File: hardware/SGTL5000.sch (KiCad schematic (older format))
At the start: 19 parts, among them J2 AudioJack3_Ground, U6 AP7313-1.8V, U7 SGTL5000

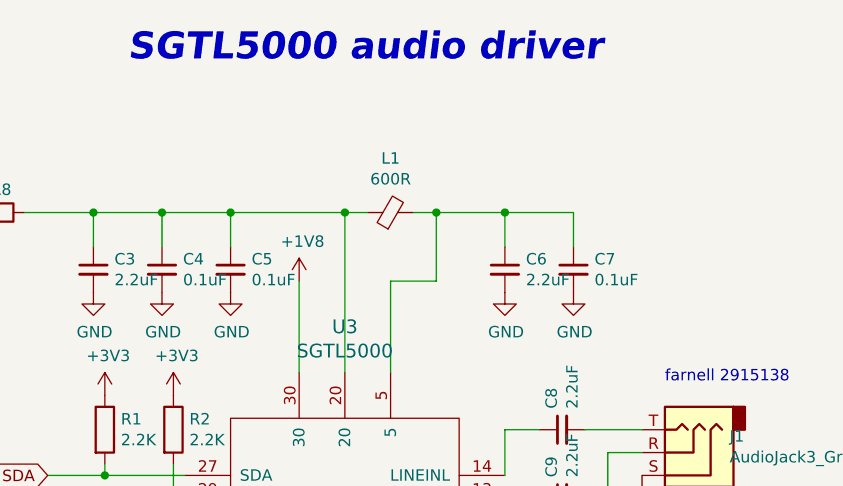
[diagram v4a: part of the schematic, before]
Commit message: new layout following feedback from pjrc forum
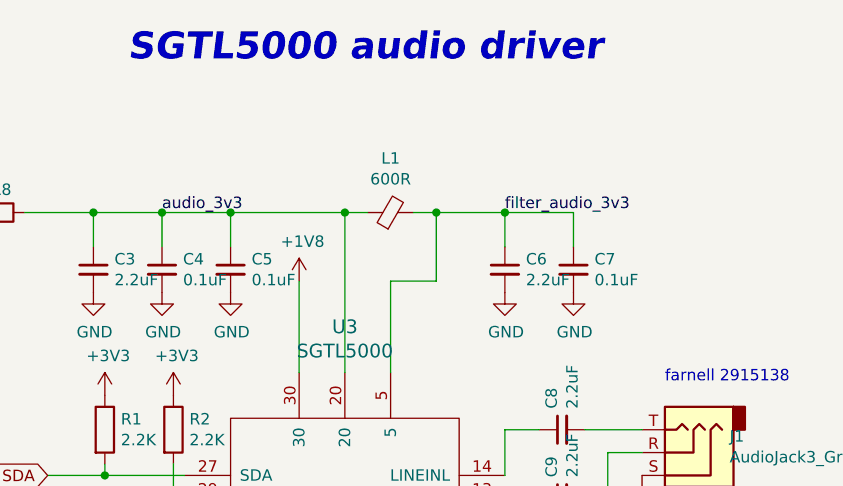
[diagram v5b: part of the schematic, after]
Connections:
- net audio_3v3: now reaches C26.1, C27.1, C28.1, L2.1, R8.1, U7.20
- net filter_audio_3v3: now reaches C29.1, C30.1, L2.2, U7.5
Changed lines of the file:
@@
-	1    0    0    -1
-$EndComp
-$Comp
-L power:GND #PWR?
-U 1 1 5BAC3E75
-P 4550 2350
-AR Path="/5BAC3E75" Ref="#PWR?"  Part="1"
-AR Path="/5BAC34FB/5BAC3E75" Ref="#PWR0128"  Part="1"
-AR Path="/5E0E3867/5BAC3E75" Ref="#PWR0108"  Part="1"
-F 0 "#PWR0108" H 4550 2100 50  0001 C CNN
-F 1 "GND" H 4555 2177 50  0000 C CNN
-F 2 "" H 4550 2350 50  0001 C CNN
-F 3 "" H 4550 2350 50  0001 C CNN
-	1    4550 2350
 	1    0    0    -1
 $EndComp
@@
 	1    0    0    -1
 $EndComp
-$Comp
-L power:GND #PWR?
-U 1 1 5BAC3E83
-P 4850 2350
-AR Path="/5BAC3E83" Ref="#PWR?"  Part="1"
-AR Path="/5BAC34FB/5BAC3E83" Ref="#PWR0129"  Part="1"
-AR Path="/5E0E3867/5BAC3E83" Ref="#PWR0109"  Part="1"
-F 0 "#PWR0109" H 4850 2100 50  0001 C CNN
-F 1 "GND" H 4855 2177 50  0000 C CNN
-F 2 "" H 4850 2350 50  0001 C CNN
-F 3 "" H 4850 2350 50  0001 C CNN
-	1    4850 2350
-	1    0    0    -1
-$EndComp
 Wire Wire Line
 	4850 2000 4850 2150
@@
 	1    0    0    -1
 $EndComp
-$Comp
-L power:GND #PWR?
-U 1 1 5BAC3E91
-P 5150 2350
-AR Path="/5BAC3E91" Ref="#PWR?"  Part="1"
-AR Path="/5BAC34FB/5BAC3E91" Ref="#PWR0130"  Part="1"
-AR Path="/5E0E3867/5BAC3E91" Ref="#PWR0110"  Part="1"
-F 0 "#PWR0110" H 5150 2100 50  0001 C CNN
-F 1 "GND" H 5155 2177 50  0000 C CNN
-F 2 "" H 5150 2350 50  0001 C CNN
-F 3 "" H 5150 2350 50  0001 C CNN
-	1    5150 2350
-	1    0    0    -1
-$EndComp
 Wire Wire Line
 	5150 2000 5150 2150
@@
 	1    0    0    -1
 $EndComp
-$Comp
-L power:GND #PWR?
-U 1 1 5BAC3E9F
-P 6350 2350
-AR Path="/5BAC3E9F" Ref="#PWR?"  Part="1"
-AR Path="/5BAC34FB/5BAC3E9F" Ref="#PWR0131"  Part="1"
-AR Path="/5E0E3867/5BAC3E9F" Ref="#PWR0111"  Part="1"
-F 0 "#PWR0111" H 6350 2100 50  0001 C CNN
-F 1 "GND" H 6355 2177 50  0000 C CNN
-F 2 "" H 6350 2350 50  0001 C CNN
-F 3 "" H 6350 2350 50  0001 C CNN
-	1    6350 2350
-	1    0    0    -1
-$EndComp
 Wire Wire Line
 	6350 2000 6350 2150
@@
 F 3 "~" H 6650 2250 50  0001 C CNN
 	1    6650 2250
-	1    0    0    -1
-$EndComp
-$Comp
-L power:GND #PWR?
-U 1 1 5BAC3EAD
-P 6650 2350
-AR Path="/5BAC3EAD" Ref="#PWR?"  Part="1"
-AR Path="/5BAC34FB/5BAC3EAD" Ref="#PWR0132"  Part="1"
-AR Path="/5E0E3867/5BAC3EAD" Ref="#PWR0112"  Part="1"
-F 0 "#PWR0112" H 6650 2100 50  0001 C CNN
-F 1 "GND" H 6655 2177 50  0000 C CNN
-F 2 "" H 6650 2350 50  0001 C CNN
-F 3 "" H 6650 2350 50  0001 C CNN
-	1    6650 2350
 	1    0    0    -1
 $EndComp
@@
 Connection ~ 6050 2000
 $Comp
-L power:GND #PWR?
-U 1 1 5BAC457F
-P 5450 5000
-AR Path="/5BAC457F" Ref="#PWR?"  Part="1"
-AR Path="/5BAC34FB/5BAC457F" Ref="#PWR0141"  Part="1"
-AR Path="/5E0E3867/5BAC457F" Ref="#PWR0115"  Part="1"
-F 0 "#PWR0115" H 5450 4750 50  0001 C CNN
-F 1 "GND" H 5455 4827 50  0000 C CNN
-F 2 "" H 5450 5000 50  0001 C CNN
-F 3 "" H 5450 5000 50  0001 C CNN
-	1    5450 5000
-	1    0    0    -1
-$EndComp
-$Comp
 L teensy_beats-cache:teensy_beats_parts_AP7313R-1.8V U?
 U 1 1 5BAC54DA
@@
 F 3 "" H 1750 2450 50  0001 C CNN
 	1    1750 2450
-	1    0    0    -1
-$EndComp
-$Comp
-L power:GND #PWR?
-U 1 1 5BAC54EE
-P 2250 2450
-AR Path="/5BAC54EE" Ref="#PWR?"  Part="1"
-AR Path="/5BAC34FB/5BAC54EE" Ref="#PWR0134"  Part="1"
-AR Path="/5E0E3867/5BAC54EE" Ref="#PWR0117"  Part="1"
-F 0 "#PWR0117" H 2250 2200 50  0001 C CNN
-F 1 "GND" H 2255 2277 50  0000 C CNN
-F 2 "" H 2250 2450 50  0001 C CNN
-F 3 "" H 2250 2450 50  0001 C CNN
-	1    2250 2450
 	1    0    0    -1
 $EndComp
@@
 $EndComp
 $Comp
-L power:GND #PWR?
-U 1 1 5E0FD89C
-P 6950 3150
-AR Path="/5E0FD89C" Ref="#PWR?"  Part="1"
-AR Path="/5BAC34FB/5E0FD89C" Ref="#PWR?"  Part="1"
-AR Path="/5E0E3867/5E0FD89C" Ref="#PWR0120"  Part="1"
-F 0 "#PWR0120" H 6950 2900 50  0001 C CNN
-F 1 "GND" H 6955 2977 50  0000 C CNN
-F 2 "" H 6950 3150 50  0001 C CNN
-F 3 "" H 6950 3150 50  0001 C CNN
-	1    6950 3150
-	1    0    0    -1
-$EndComp
-$Comp
 L Device:C_Small C?
 U 1 1 5E0FEC6F
@@
 Wire Wire Line
 	4950 4100 4450 4100
-$Comp
-L power:GND #PWR?
-U 1 1 5E1010DB
-P 4450 4300
-AR Path="/5E1010DB" Ref="#PWR?"  Part="1"
-AR Path="/5BAC34FB/5E1010DB" Ref="#PWR?"  Part="1"
-AR Path="/5E0E3867/5E1010DB" Ref="#PWR0122"  Part="1"
-F 0 "#PWR0122" H 4450 4050 50  0001 C CNN
-F 1 "GND" H 4455 4127 50  0000 C CNN
-F 2 "" H 4450 4300 50  0001 C CNN
-F 3 "" H 4450 4300 50  0001 C CNN
-	1    4450 4300
-	1    0    0    -1
-$EndComp
 NoConn ~ 4950 4200
 NoConn ~ 6350 4300
@@
 F 3 "" H 6650 4350 50  0001 C CNN
 	1    6650 4350
+	1    0    0    -1
+$EndComp
+$Comp
+L power:GND #PWR?
+U 1 1 5BAC54EE
+P 2250 2450
+AR Path="/5BAC54EE" Ref="#PWR?"  Part="1"
+AR Path="/5BAC34FB/5BAC54EE" Ref="#PWR0134"  Part="1"
+AR Path="/5E0E3867/5BAC54EE" Ref="#PWR0117"  Part="1"
+F 0 "#PWR0117" H 2250 2200 50  0001 C CNN
+F 1 "GND" H 2255 2277 50  0000 C CNN
+F 2 "" H 2250 2450 50  0001 C CNN
+F 3 "" H 2250 2450 50  0001 C CNN
+	1    2250 2450
+	1    0    0    -1
+$EndComp
+$Comp
+L power:GND #PWR?
+U 1 1 5BAC3EAD
+P 6650 2350
+AR Path="/5BAC3EAD" Ref="#PWR?"  Part="1"
+AR Path="/5BAC34FB/5BAC3EAD" Ref="#PWR0132"  Part="1"
+AR Path="/5E0E3867/5BAC3EAD" Ref="#PWR0112"  Part="1"
+F 0 "#PWR0112" H 6650 2100 50  0001 C CNN
+F 1 "GND" H 6655 2177 50  0000 C CNN
+F 2 "" H 6650 2350 50  0001 C CNN
+F 3 "" H 6650 2350 50  0001 C CNN
+	1    6650 2350
+	1    0    0    -1
+$EndComp
+$Comp
+L power:GND #PWR?
+U 1 1 5BAC3E9F
+P 6350 2350
+AR Path="/5BAC3E9F" Ref="#PWR?"  Part="1"
+AR Path="/5BAC34FB/5BAC3E9F" Ref="#PWR0131"  Part="1"
+AR Path="/5E0E3867/5BAC3E9F" Ref="#PWR0111"  Part="1"
+F 0 "#PWR0111" H 6350 2100 50  0001 C CNN
+F 1 "GND" H 6355 2177 50  0000 C CNN
+F 2 "" H 6350 2350 50  0001 C CNN
+F 3 "" H 6350 2350 50  0001 C CNN
+	1    6350 2350
+	1    0    0    -1
+$EndComp
+$Comp
+L power:GND #PWR?
+U 1 1 5BAC3E91
+P 5150 2350
+AR Path="/5BAC3E91" Ref="#PWR?"  Part="1"
+AR Path="/5BAC34FB/5BAC3E91" Ref="#PWR0130"  Part="1"
+AR Path="/5E0E3867/5BAC3E91" Ref="#PWR0110"  Part="1"
+F 0 "#PWR0110" H 5150 2100 50  0001 C CNN
+F 1 "GND" H 5155 2177 50  0000 C CNN
+F 2 "" H 5150 2350 50  0001 C CNN
+F 3 "" H 5150 2350 50  0001 C CNN
+	1    5150 2350
+	1    0    0    -1
+$EndComp
+$Comp
+L power:GND #PWR?
+U 1 1 5BAC3E83
+P 4850 2350
+AR Path="/5BAC3E83" Ref="#PWR?"  Part="1"
+AR Path="/5BAC34FB/5BAC3E83" Ref="#PWR0129"  Part="1"
+AR Path="/5E0E3867/5BAC3E83" Ref="#PWR0109"  Part="1"
+F 0 "#PWR0109" H 4850 2100 50  0001 C CNN
+F 1 "GND" H 4855 2177 50  0000 C CNN
+F 2 "" H 4850 2350 50  0001 C CNN
+F 3 "" H 4850 2350 50  0001 C CNN
+	1    4850 2350
+	1    0    0    -1
+$EndComp
+$Comp
+L power:GND #PWR?
+U 1 1 5BAC3E75
+P 4550 2350
+AR Path="/5BAC3E75" Ref="#PWR?"  Part="1"
+AR Path="/5BAC34FB/5BAC3E75" Ref="#PWR0128"  Part="1"
+AR Path="/5E0E3867/5BAC3E75" Ref="#PWR0108"  Part="1"
+F 0 "#PWR0108" H 4550 2100 50  0001 C CNN
+F 1 "GND" H 4555 2177 50  0000 C CNN
+F 2 "" H 4550 2350 50  0001 C CNN
+F 3 "" H 4550 2350 50  0001 C CNN
+	1    4550 2350
+	1    0    0    -1
+$EndComp
+$Comp
+L power:GND #PWR?
+U 1 1 5E1010DB
+P 4450 4300
+AR Path="/5E1010DB" Ref="#PWR?"  Part="1"
+AR Path="/5BAC34FB/5E1010DB" Ref="#PWR?"  Part="1"
+AR Path="/5E0E3867/5E1010DB" Ref="#PWR0122"  Part="1"
+F 0 "#PWR0122" H 4450 4050 50  0001 C CNN
+F 1 "GND" H 4455 4127 50  0000 C CNN
+F 2 "" H 4450 4300 50  0001 C CNN
+F 3 "" H 4450 4300 50  0001 C CNN
+	1    4450 4300
+	1    0    0    -1
+$EndComp
+$Comp
+L power:GND #PWR?
+U 1 1 5BAC457F
+P 5450 5000
+AR Path="/5BAC457F" Ref="#PWR?"  Part="1"
+AR Path="/5BAC34FB/5BAC457F" Ref="#PWR0141"  Part="1"
+AR Path="/5E0E3867/5BAC457F" Ref="#PWR0115"  Part="1"
+F 0 "#PWR0115" H 5450 4750 50  0001 C CNN
+F 1 "GND" H 5455 4827 50  0000 C CNN
+F 2 "" H 5450 5000 50  0001 C CNN
+F 3 "" H 5450 5000 50  0001 C CNN
+	1    5450 5000
+	1    0    0    -1
+$EndComp
+$Comp
+L power:GND #PWR?
+U 1 1 5E0FD89C
+P 6950 3150
+AR Path="/5E0FD89C" Ref="#PWR?"  Part="1"
+AR Path="/5BAC34FB/5E0FD89C" Ref="#PWR?"  Part="1"
+AR Path="/5E0E3867/5E0FD89C" Ref="#PWR0120"  Part="1"
+F 0 "#PWR0120" H 6950 2900 50  0001 C CNN
+F 1 "GND" H 6955 2977 50  0000 C CNN
+F 2 "" H 6950 3150 50  0001 C CNN
+F 3 "" H 6950 3150 50  0001 C CNN
+	1    6950 3150
 	1    0    0    -1
 $EndComp
@@
 	0    1    1    0
 $EndComp
+Text Label 4850 2000 0    50   ~ 0
+audio_3v3
+Text Label 6350 2000 0    50   ~ 0
+filter_audio_3v3
 $EndSCHEMATC

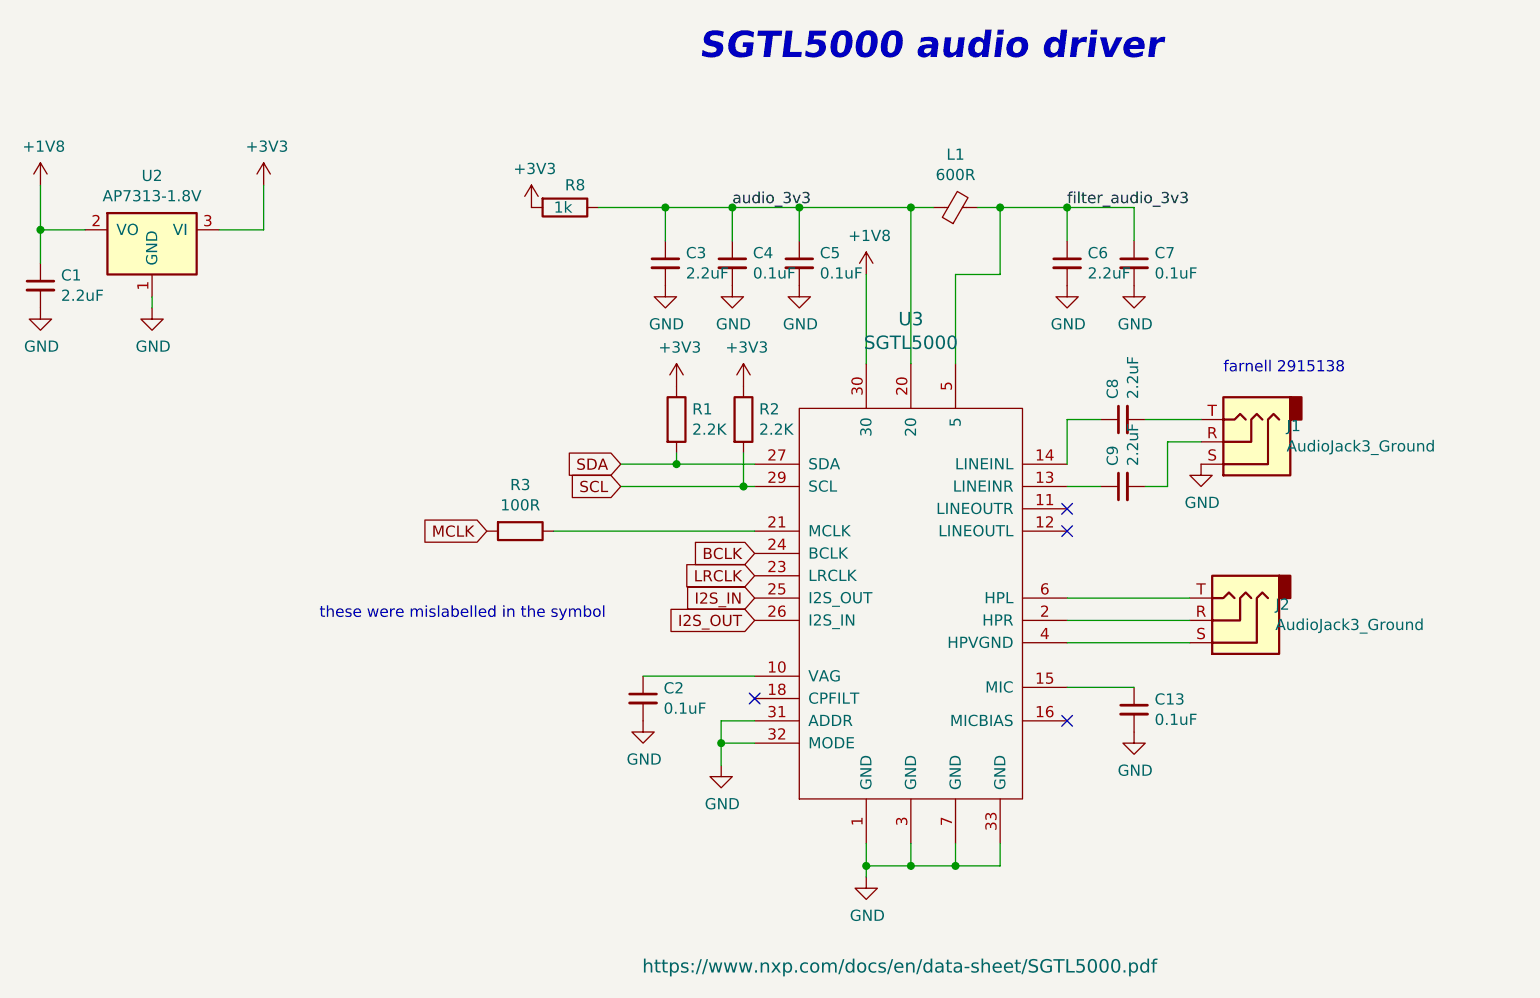
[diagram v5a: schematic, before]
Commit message: changed 3v3 to gnd plane under audio circuitry, added lineout jack
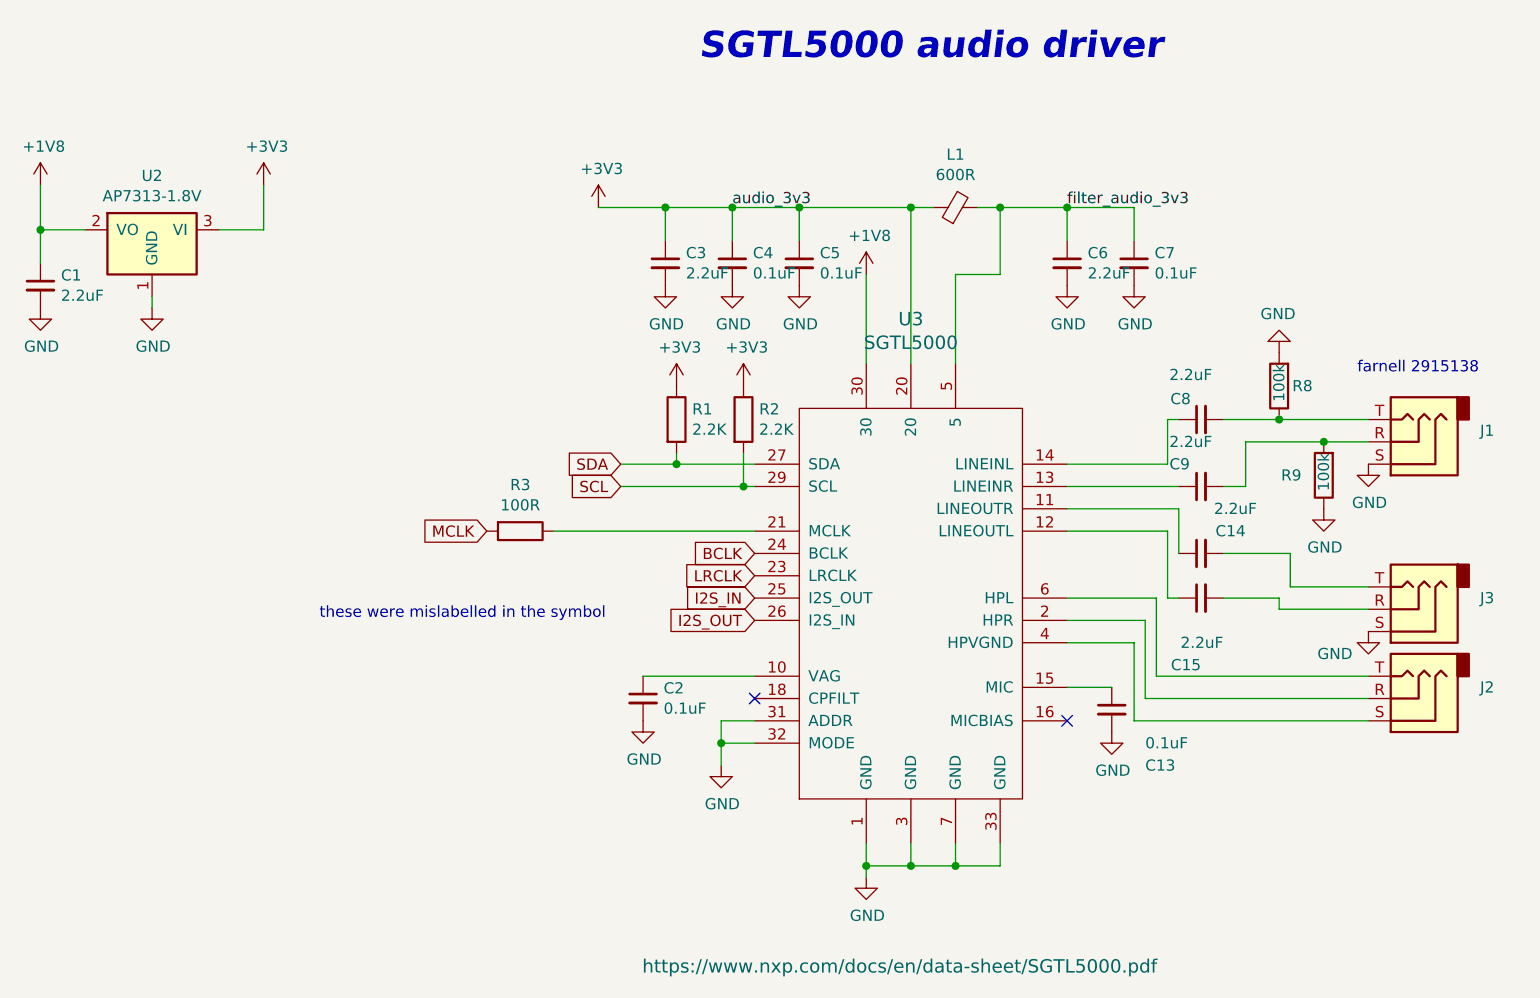
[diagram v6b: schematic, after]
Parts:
- added C14, C15: 2.2uF, Capacitor_SMD:C_0805_2012Metric, symbol Device:C_Small
- added J3: AudioJack3_Ground, Connector_Audio:Jack_3.5mm_CUI_SJ-3523-SMT_Horizontal, symbol Connector:AudioJack3
- added R9: 100k, Resistor_SMD:R_0805_2012Metric, symbol Device:R
- R8: value 1k -> 100k
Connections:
- net +3V3: now also C26.1, C27.1, C28.1, L2.1, U7.20; no longer R8.2
- net GND: now also R8.2, J3.S, R9.1
- net at U7.11 (LINEOUTR): now also C14.1
- net at U7.12 (LINEOUTL): now also C15.1
- net at C9.2, J2.R: now also R9.2
- net at C8.2, J2.T: now also R8.1
- removed net audio_3v3: C26.1, C27.1, C28.1, L2.1, R8.1, U7.20
- new net: C15.2, J3.R
- new net: C14.2, J3.T
- no-connect marks 4 -> 2
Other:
- moved on the sheet: C13, C8, C9, J1, J2, R8

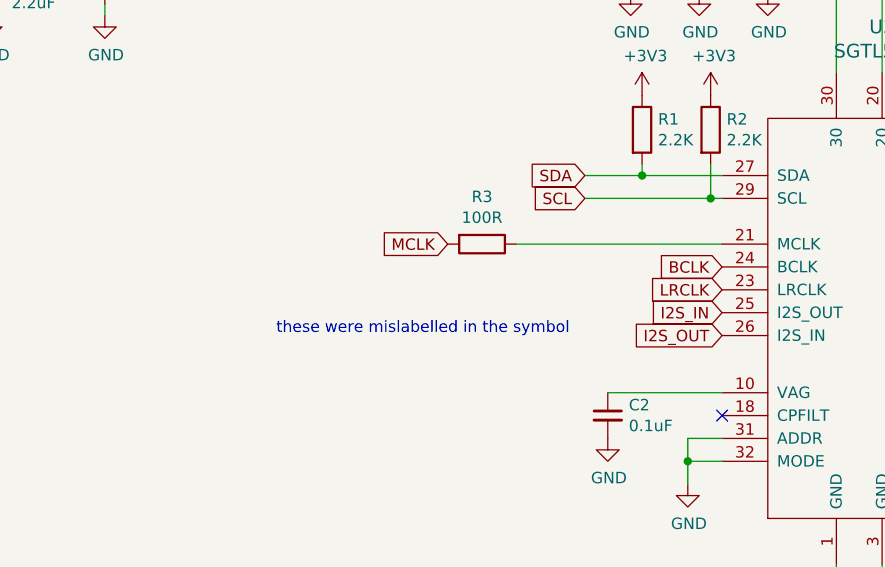
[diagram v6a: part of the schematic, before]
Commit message: try adding resistors to all the i2s lines
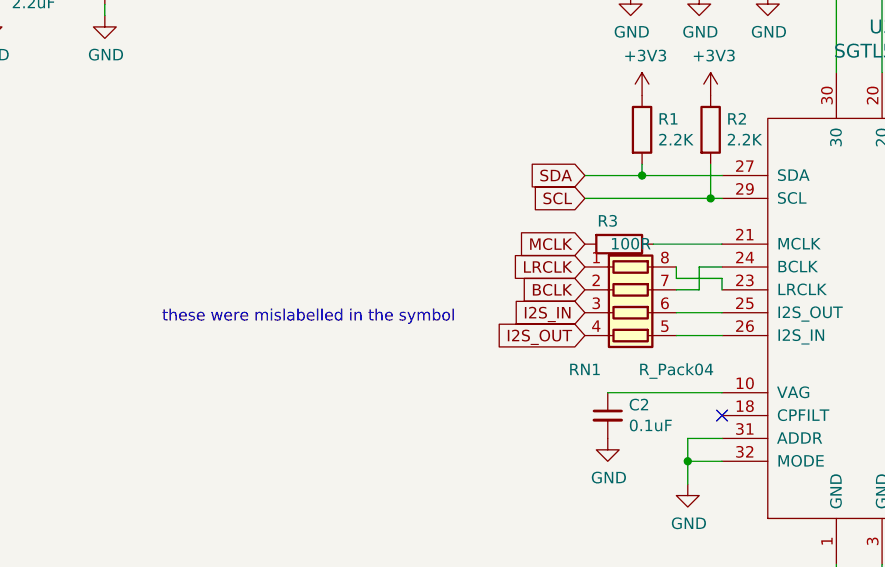
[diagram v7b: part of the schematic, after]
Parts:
- added RN1: R_Pack04, Resistor_SMD:R_Array_Convex_4x0603, symbol Device:R_Pack04
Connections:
- net BCLK: now also RN1.2 (R2.1); no longer U7.24 (BCLK)
- net I2S_IN: now also RN1.3 (R3.1); no longer U7.25 (I2S_OUT)
- net I2S_OUT: now also RN1.4 (R4.1); no longer U7.26 (I2S_IN)
- net LRCLK: now also RN1.1 (R1.1); no longer U7.23 (LRCLK)
- new net: RN1.8 (R1.2), U7.23 (LRCLK)
- new net: RN1.7 (R2.2), U7.24 (BCLK)
- new net: RN1.6 (R3.2), U7.25 (I2S_OUT)
- new net: RN1.5 (R4.2), U7.26 (I2S_IN)
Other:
- moved on the sheet: R3
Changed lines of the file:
@@
 Text GLabel 4350 3250 0    50   Input ~ 0
 SCL
-Text GLabel 3750 3450 0    50   Input ~ 0
+Text GLabel 4350 3450 0    50   Input ~ 0
 MCLK
-Text GLabel 4950 3550 0    50   Input ~ 0
+Text GLabel 4350 3650 0    50   Input ~ 0
 BCLK
-Text GLabel 4950 3650 0    50   Input ~ 0
+Text GLabel 4350 3550 0    50   Input ~ 0
 LRCLK
-Text GLabel 4950 3750 0    50   Input ~ 0
+Text GLabel 4350 3750 0    50   Input ~ 0
 I2S_IN
-Text GLabel 4950 3850 0    50   Input ~ 0
+Text GLabel 4350 3850 0    50   Input ~ 0
 I2S_OUT
 Wire Wire Line
@@
 L Device:R R?
 U 1 1 5E21D79E
-P 3900 3450
+P 4500 3450
 AR Path="/5E21D79E" Ref="R?"  Part="1"
 AR Path="/5E0E3867/5E21D79E" Ref="R3"  Part="1"
-F 0 "R3" V 3693 3450 50  0000 C CNN
-F 1 "100R" V 3784 3450 50  0000 C CNN
-F 2 "Resistor_SMD:R_0805_2012Metric" V 3830 3450 50  0001 C CNN
-F 3 "~" H 3900 3450 50  0001 C CNN
-	1    3900 3450
+F 0 "R3" V 4400 3400 50  0000 C CNN
+F 1 "100R" V 4500 3500 50  0000 C CNN
+F 2 "Resistor_SMD:R_0805_2012Metric" V 4430 3450 50  0001 C CNN
+F 3 "~" H 4500 3450 50  0001 C CNN
+	1    4500 3450
 	0    1    1    0
 $EndComp
-Wire Wire Line
-	4050 3450 4950 3450
 Text Notes 4700 1350 0    118  Italic 24
 SGTL5000 audio driver
-Text Notes 3000 3850 0    50   ~ 0
+Text Notes 2500 3800 0    50   ~ 0
 these were mislabelled in the symbol\n
 $Comp
@@
 Wire Wire Line
 	6650 4300 7700 4300
+$Comp
+L Device:R_Pack04 RN1
+U 1 1 5E1364CA
+P 4550 3750
+F 0 "RN1" V 4800 3550 50  0000 C CNN
+F 1 "R_Pack04" V 4800 3950 50  0000 C CNN
+F 2 "Resistor_SMD:R_Array_Convex_4x0603" V 4825 3750 50  0001 C CNN
+F 3 "~" H 4550 3750 50  0001 C CNN
+	1    4550 3750
+	0    1    1    0
+$EndComp
+Wire Wire Line
+	4650 3450 4950 3450
+Wire Wire Line
+	4750 3750 4950 3750
+Wire Wire Line
+	4750 3850 4950 3850
+Wire Wire Line
+	4850 3650 4850 3550
+Wire Wire Line
+	4850 3550 4950 3550
+Wire Wire Line
+	4750 3650 4850 3650
+Wire Wire Line
+	4750 3550 4750 3600
+Wire Wire Line
+	4750 3600 4950 3600
+Wire Wire Line
+	4950 3600 4950 3650
 $EndSCHEMATC
